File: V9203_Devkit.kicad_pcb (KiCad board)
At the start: 2 copper layers, 50 x 50 mm, 50 parts, among them J1 RJ45, J2 CONN_01X16, J3 CONN_01X12, J4 Screw_Terminal_1x04, J5 GROVE-CONNECTOR-SMD-90D(4+2P-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, U1 V9203, U2 ROF-78E, Y1 Crystal_GND24

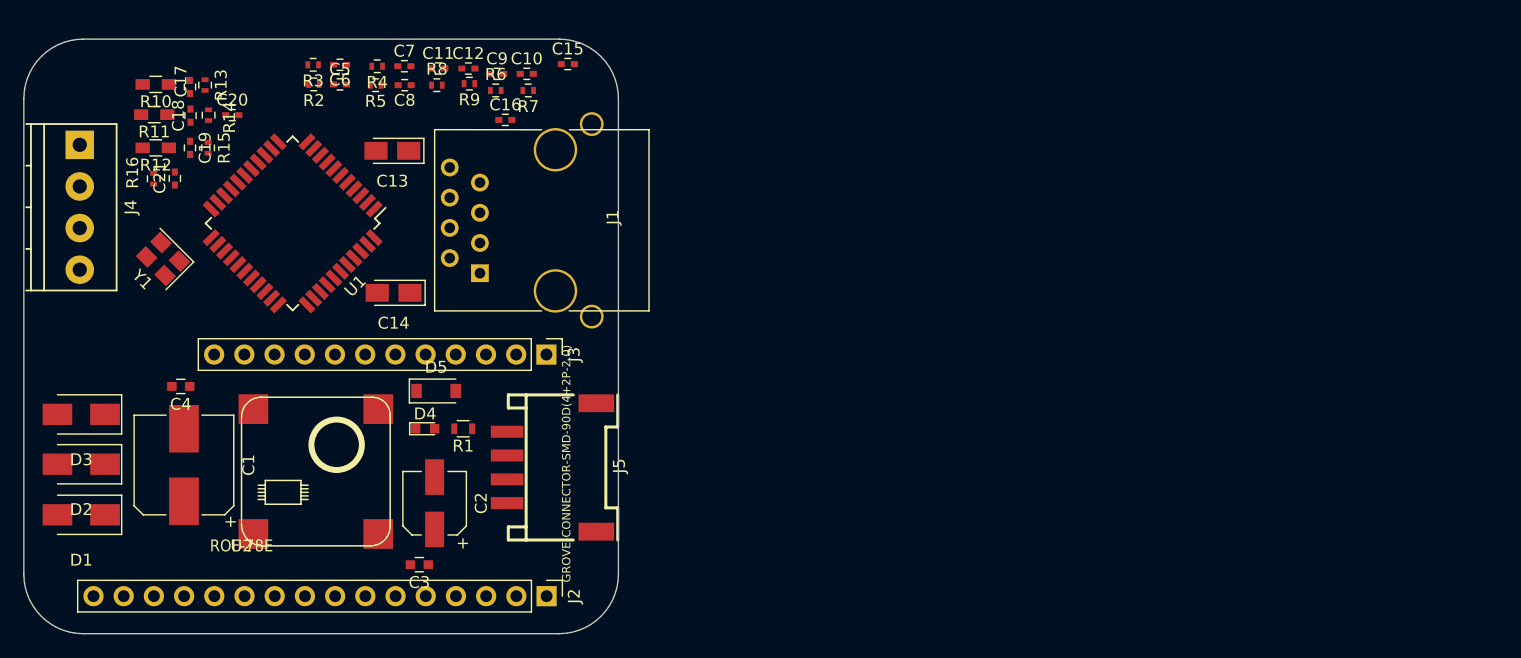
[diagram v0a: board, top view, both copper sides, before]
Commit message: Added more parts to featherwing
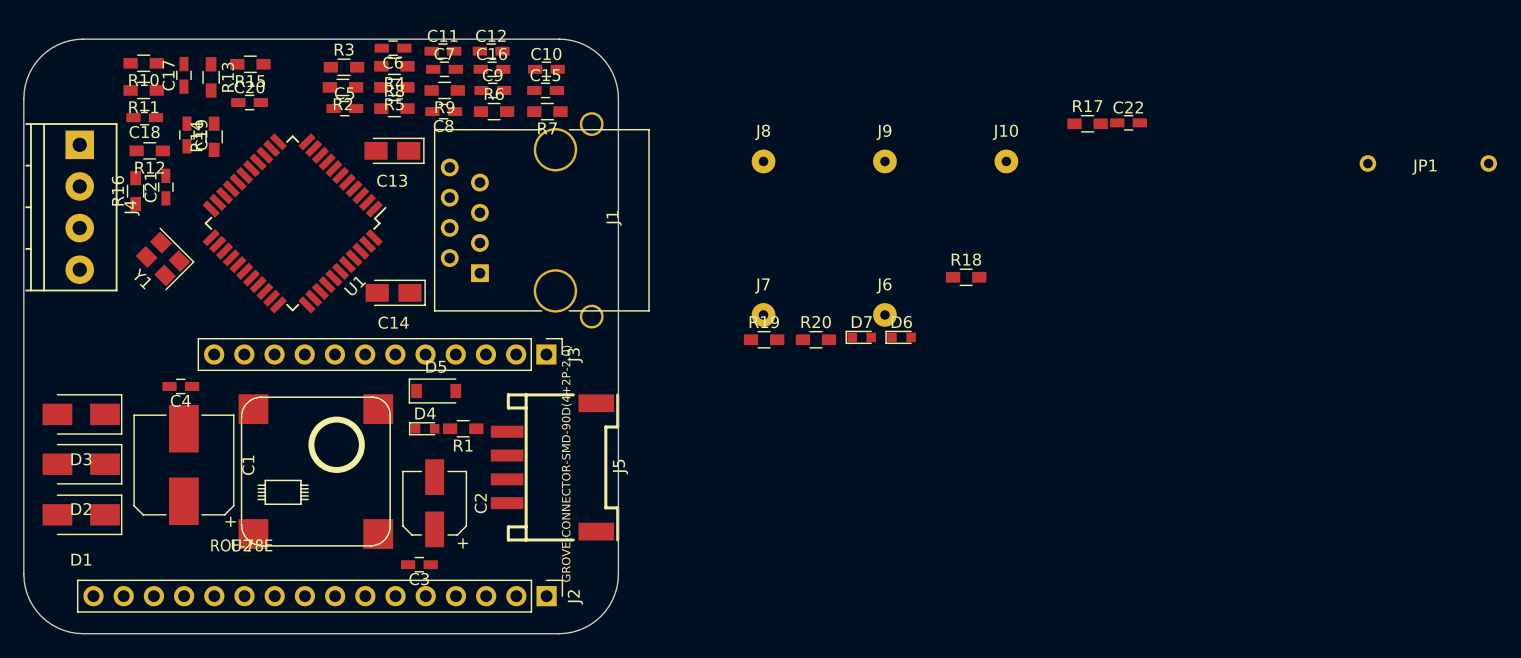
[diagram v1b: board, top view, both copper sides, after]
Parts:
- added C22: C, Capacitors_SMD:C_0603_HandSoldering, F.Cu at (202.9, 47.0)
- added D6: LED, LEDs:LED_0603, F.Cu at (183.8, 65.1)
- added D7: LED, LEDs:LED_0603, F.Cu at (180.5, 65.1)
- added J10: CONN_01X01, Wire_Pads:SolderWirePad_single_0-8mmDrill, F.Cu at (192.6, 50.3)
- added J6: CONN_01X01, Wire_Pads:SolderWirePad_single_0-8mmDrill, F.Cu at (182.4, 63.2)
- added J7: CONN_01X01, Wire_Pads:SolderWirePad_single_0-8mmDrill, F.Cu at (172.2, 63.2)
- added J8: CONN_01X01, Wire_Pads:SolderWirePad_single_0-8mmDrill, F.Cu at (172.2, 50.3)
- added J9: CONN_01X01, Wire_Pads:SolderWirePad_single_0-8mmDrill, F.Cu at (182.4, 50.3)
- added JP1: Jumper_NC_Small, Wire_Connections_Bridges:WireConnection_0.80mmDrill_ThinPad, F.Cu at (223.0, 50.5)
- added R17: R, Resistors_SMD:R_0603_HandSoldering, F.Cu at (199.5, 47.1)
- added R18: R, Resistors_SMD:R_0603_HandSoldering, F.Cu at (189.2, 60.0)
- added R19: R, Resistors_SMD:R_0603_HandSoldering, F.Cu at (172.3, 65.3)
- added R20: R, Resistors_SMD:R_0603_HandSoldering, F.Cu at (176.6, 65.3)
- C10, C11, C12, C15, C16, C17, C18, C19, C20, C21, C5, C6, C7, C8, C9: footprint Capacitors_SMD:C_0402 -> Capacitors_SMD:C_0603_HandSoldering
- C3, C4: footprint Capacitors_SMD:C_0603 -> Capacitors_SMD:C_0603_HandSoldering
- R1: footprint Resistors_SMD:R_0603 -> Resistors_SMD:R_0603_HandSoldering
- R13, R14, R15, R16, R2, R3, R4, R5, R6, R7, R8, R9: footprint Resistors_SMD:R_0402 -> Resistors_SMD:R_0603_HandSoldering
- moved R15 7.88 mm to (129.1, 42.1), turned to 180 degrees
- moved C6 4.68 mm to (141.1, 40.8)
- moved C16 4.40 mm to (149.4, 42.5)
- moved R8 4.08 mm to (141.2, 45.8)
- moved C8 3.96 mm to (145.3, 46.1)
- moved C18 3.86 mm to (120.2, 46.6), turned to 180 degrees
- moved C7 3.38 mm to (145.4, 42.5)
- moved C15 2.90 mm to (153.9, 44.3)
- moved R3 2.61 mm to (136.9, 42.4), turned to 0 degrees
- moved R2 2.47 mm to (136.8, 44.1)
- moved C12 2.42 mm to (149.3, 41.0)
- moved R7 2.40 mm to (154.0, 46.1)
- moved R11 2.22 mm to (120.1, 44.3)
- moved R9 2.16 mm to (145.4, 44.3)
- moved C5 2.07 mm to (137.0, 45.8)
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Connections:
- U1 pad 18: Net-(U1-Pad18) -> GND
- U1 pad 20: Net-(U1-Pad20) -> GND

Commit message: Laid out most parts within PCB bounds
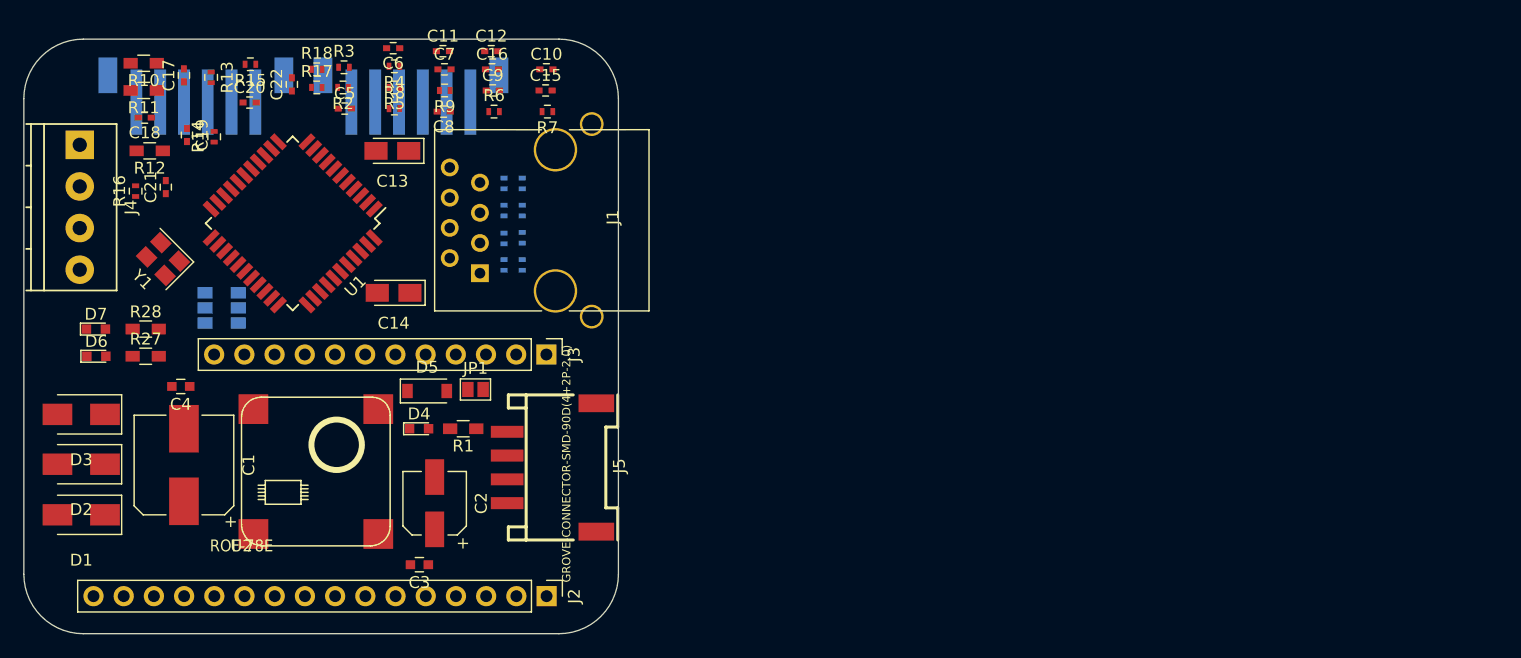
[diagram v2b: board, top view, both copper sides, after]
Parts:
- removed J10: CONN_01X01, Wire_Pads:SolderWirePad_single_0-8mmDrill
- added R21: R, Resistors_SMD:R_0402, B.Cu at (151.9, 52.1)
- added R22: R, Resistors_SMD:R_0402, B.Cu at (150.4, 59.0)
- added R23: R, Resistors_SMD:R_0402, B.Cu at (150.4, 56.8)
- added R24: R, Resistors_SMD:R_0402, B.Cu at (151.9, 59.0)
- added R25: R, Resistors_SMD:R_0402, B.Cu at (151.9, 54.4)
- added R26: R, Resistors_SMD:R_0402, B.Cu at (151.9, 56.7)
- added R27: R, Resistors_SMD:R_0603_HandSoldering, F.Cu at (120.2, 66.7)
- added R28: R, Resistors_SMD:R_0603_HandSoldering, F.Cu at (120.2, 64.4)
- C10, C11, C12, C15, C16, C17, C18, C19, C20, C21, C22, C5, C6, C7, C8, C9: footprint Capacitors_SMD:C_0603_HandSoldering -> Capacitors_SMD:C_0402
- C3, C4: footprint Capacitors_SMD:C_0603_HandSoldering -> Capacitors_SMD:C_0603
- J6, J9: value CONN_01X01 -> CONN_01X06; footprint Wire_Pads:SolderWirePad_single_0-8mmDrill -> Connectors_JST:JST_PH_B6B-PH-SM4-TB_06x2.00mm_Straight; moved to B.Cu
- J7, J8: value CONN_01X01 -> GS3; footprint Wire_Pads:SolderWirePad_single_0-8mmDrill -> Connect:GS3; moved to B.Cu
- JP1: footprint Wire_Connections_Bridges:WireConnection_0.80mmDrill_ThinPad -> Connect:GS2
- R13, R14, R15, R16, R17, R18, R2, R3, R4, R5, R6, R7, R8, R9: footprint Resistors_SMD:R_0603_HandSoldering -> Resistors_SMD:R_0402
- R19, R20: footprint Resistors_SMD:R_0603_HandSoldering -> Resistors_SMD:R_0402; moved to B.Cu
- moved JP1 77.4 mm to (148.0, 69.5), turned to 90 degrees
- moved C22 70.4 mm to (132.5, 43.8), turned to 90 degrees
- moved D6 67.7 mm to (116.1, 66.7)
- moved R17 64.9 mm to (134.6, 44.1)
- moved D7 64.4 mm to (116.1, 64.4)
- moved J9 58.3 mm to (124.5, 44.2), turned to 180 degrees
- moved R18 57.3 mm to (134.6, 42.5)
- moved J8 48.6 mm to (125.2, 62.6)
- moved J6 44.2 mm to (142.5, 44.2), turned to 180 degrees
- moved J7 44.2 mm to (128.0, 62.6)
- moved R20 28.4 mm to (150.4, 54.4), turned to 90 degrees
- moved R19 25.5 mm to (150.4, 52.1), turned to 270 degrees
- moved D5 0.76 mm to (143.9, 69.6)
- moved D4 0.51 mm to (143.2, 72.8)
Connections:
- J8 pad 1: Net-(J8-Pad1) -> Net-(J7-Pad1)
- J9 pad 1: Net-(J9-Pad1) -> CS
- R17 pad 1: Net-(C22-Pad2) -> GND
- R17 pad 2: Net-(R17-Pad2) -> /V9203/IAN_IN
- R18 pad 1: GND -> /V9203/IAP_IN
- R18 pad 2: Net-(C22-Pad2) -> GND
- R19 pad 1: Net-(D6-Pad2) -> GND
- R19 pad 2: Net-(R19-Pad2) -> /V9203/ICN_IN
- R20 pad 1: Net-(D7-Pad2) -> /V9203/ICP_IN
- R20 pad 2: Net-(R20-Pad2) -> GND
- U1 pad 24: Net-(U1-Pad24) -> Net-(J8-Pad2)
- U1 pad 25: Net-(U1-Pad25) -> Net-(J7-Pad2)
- U1 pad 26: Net-(R20-Pad2) -> Net-(R28-Pad2)
- U1 pad 27: Net-(R19-Pad2) -> Net-(R27-Pad2)
- U1 pad 30: Net-(J10-Pad1) -> Net-(J6-Pad5)
- U1 pad 31: Net-(J9-Pad1) -> Net-(J6-Pad4)
- U1 pad 32: Net-(J8-Pad1) -> Net-(J6-Pad3)
- U1 pad 33: Net-(J7-Pad1) -> Net-(J6-Pad2)

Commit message: Neaten up parts layout
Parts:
- added C23: C, Capacitors_SMD:C_0402, F.Cu at (136.4, 63.9)
- added C24: C, Capacitors_SMD:C_0402, F.Cu at (138.7, 63.9)
- added C25: C, Capacitors_SMD:C_0402, F.Cu at (141.2, 63.9)
- added C26: C, Capacitors_SMD:C_0402, F.Cu at (143.5, 63.9)
- added R29: R, Resistors_SMD:R_0402, F.Cu at (139.3, 62.2)
- added R30: R, Resistors_SMD:R_0402, F.Cu at (137.2, 62.2)
- added R31: R, Resistors_SMD:R_0402, F.Cu at (141.2, 62.2)
- added R32: R, Resistors_SMD:R_0402, F.Cu at (143.1, 62.2)
- R17, R18: footprint Resistors_SMD:R_0402 -> Resistors_SMD:R_0603; moved to B.Cu
- R19, R20, R21, R22, R23, R24: footprint Resistors_SMD:R_0402 -> Resistors_SMD:R_0603
- R25, R26: moved to F.Cu
- moved R18 24.1 mm to (154.5, 56.3)
- moved R17 22.4 mm to (154.5, 54.5)
- moved R26 16.9 mm to (138.8, 46.1), turned to 180 degrees
- moved R25 16.3 mm to (138.8, 44.8), turned to 180 degrees
- moved R16 9.45 mm to (126.4, 46.4), turned to 180 degrees
- moved C7 9.30 mm to (136.1, 42.4)
- moved R7 8.29 mm to (146.1, 43.6)
- moved C12 7.66 mm to (143.6, 46.1)
- moved C6 7.30 mm to (136.1, 46.1)
- moved C21 6.19 mm to (123.7, 46.5), turned to 180 degrees
- moved C20 5.93 mm to (123.8, 48.1)
- moved C9 5.89 mm to (143.6, 44.8)
- moved C10 5.37 mm to (148.7, 43.4)
- moved C15 5.29 mm to (148.6, 44.8)
- moved R6 5.20 mm to (146.1, 42.2)
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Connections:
- J7 pad 1: Net-(J7-Pad1) -> +3V3
- J8 pad 1: Net-(J7-Pad1) -> +3V3
- R25 pad 2: Net-(R25-Pad2) -> +3V3
- U1 pad 38: CS -> /V9203/V_CS
- U1 pad 39: SCK -> /V9203/V_CLK
- U1 pad 40: MISO -> /V9203/V_MISO
- U1 pad 41: MOSI -> /V9203/V_MOSI

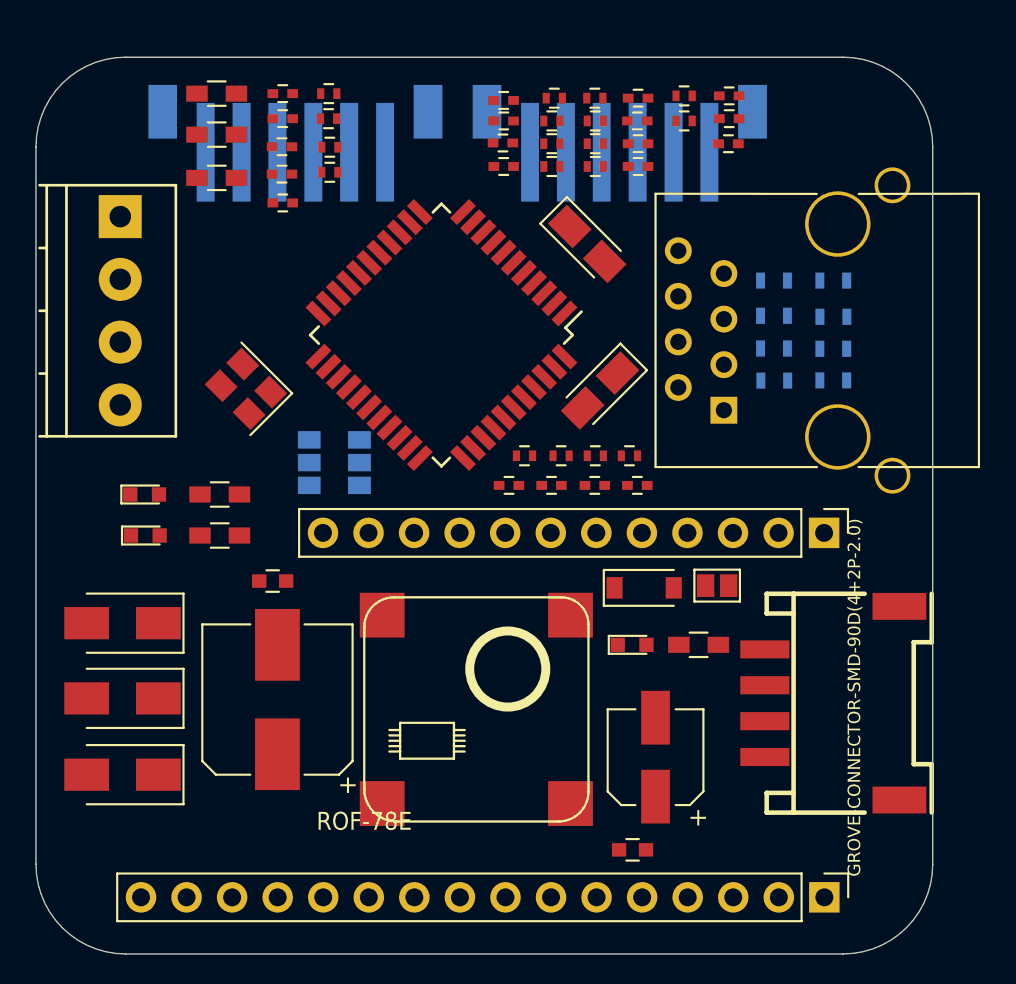
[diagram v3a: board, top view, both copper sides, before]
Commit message: Added JST footprints, mounting holes and logos
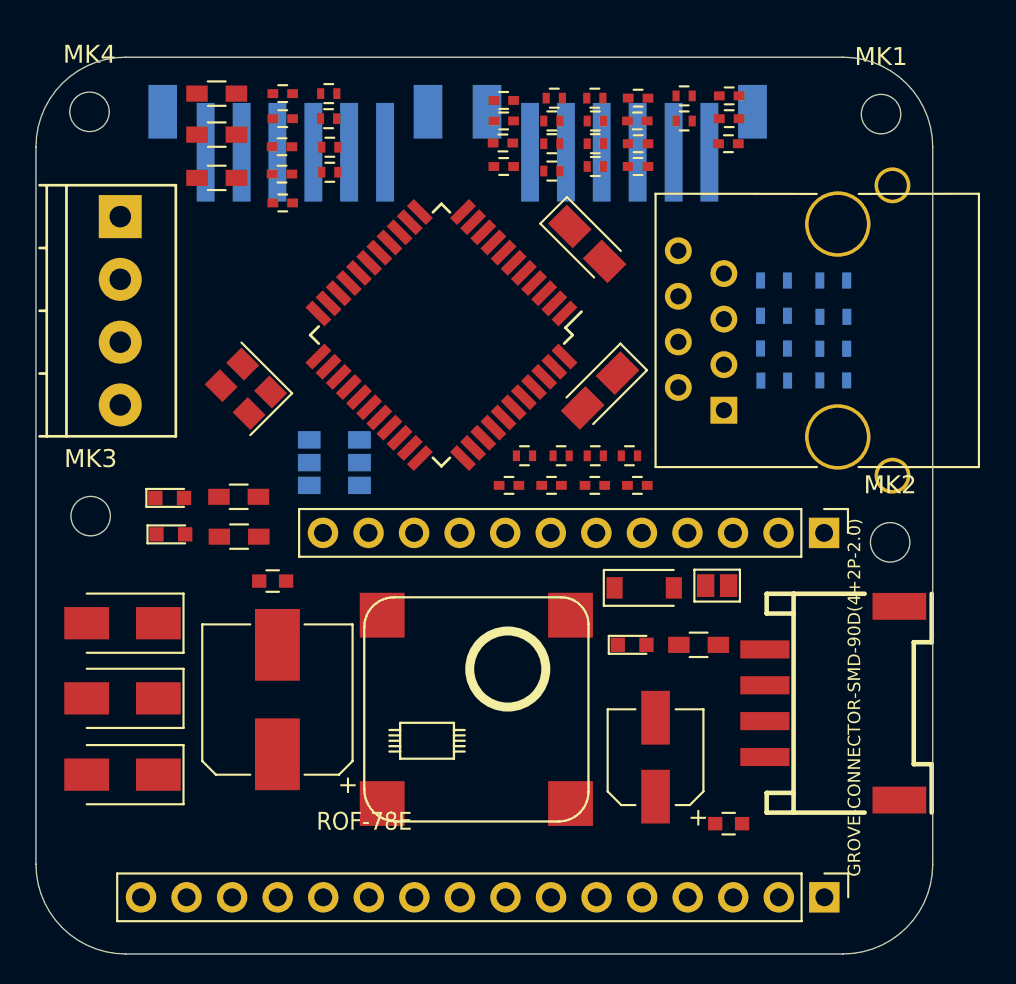
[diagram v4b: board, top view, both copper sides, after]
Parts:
- added LOGO1: OPEN_HARDWARE_1, Symbols:OSHW-Logo2_7.3x6mm_SilkScreen, B.Cu at (134.6, 76.6)
- added MK1: Mounting_Hole, Mounting_Holes:MountingHole_2.2mm_M2, F.Cu at (157.1, 43.2)
- added MK2: Mounting_Hole, Mounting_Holes:MountingHole_2.2mm_M2, F.Cu at (157.6, 67.0)
- added MK3: Mounting_Hole, Mounting_Holes:MountingHole_2.2mm_M2, F.Cu at (113.0, 65.6)
- added MK4: Mounting_Hole, Mounting_Holes:MountingHole_2.2mm_M2, F.Cu at (113.0, 43.0)
- moved C3 5.55 mm to (148.6, 82.7)
- moved D6 1.42 mm to (117.5, 66.6)
- moved D7 1.41 mm to (117.5, 64.6)
- moved R27 1.08 mm to (121.3, 66.7)
- moved R28 1.07 mm to (121.3, 64.5)
- moved R26 0.25 mm to (138.8, 46.3)
